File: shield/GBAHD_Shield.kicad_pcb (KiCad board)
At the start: 2 copper layers, 79.5 x 64.4 mm, 70 parts, among them J1 Conn_01x40, J10 Conn_01x02, J11 Conn_01x05, J2 Conn_02x08_Top_Bottom, J3 Conn_01x20, J4 Conn_02x10_Top_Bottom, J5 Conn_01x34, J6 Conn_02x03_Odd_Even, J7 Conn_01x32, J8 Conn_01x05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

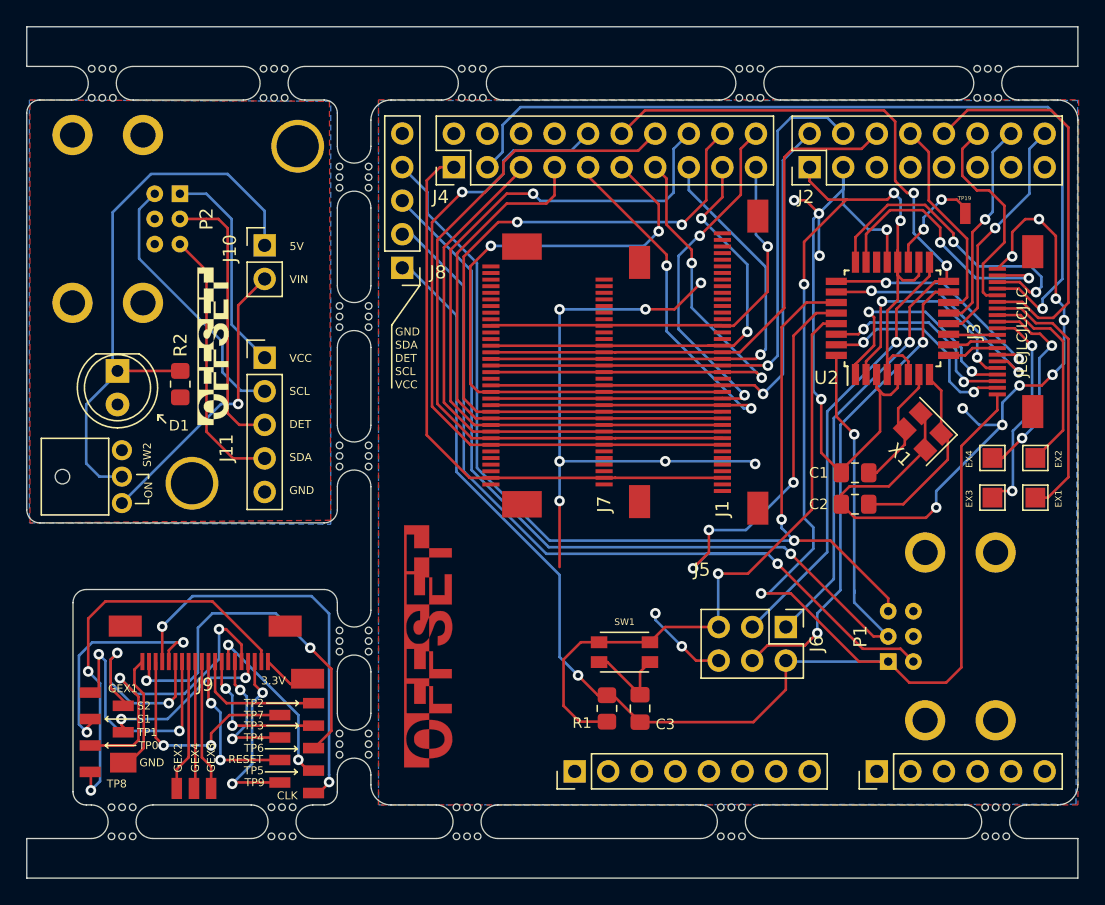
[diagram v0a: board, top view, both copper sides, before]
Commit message: Fixed moved traces
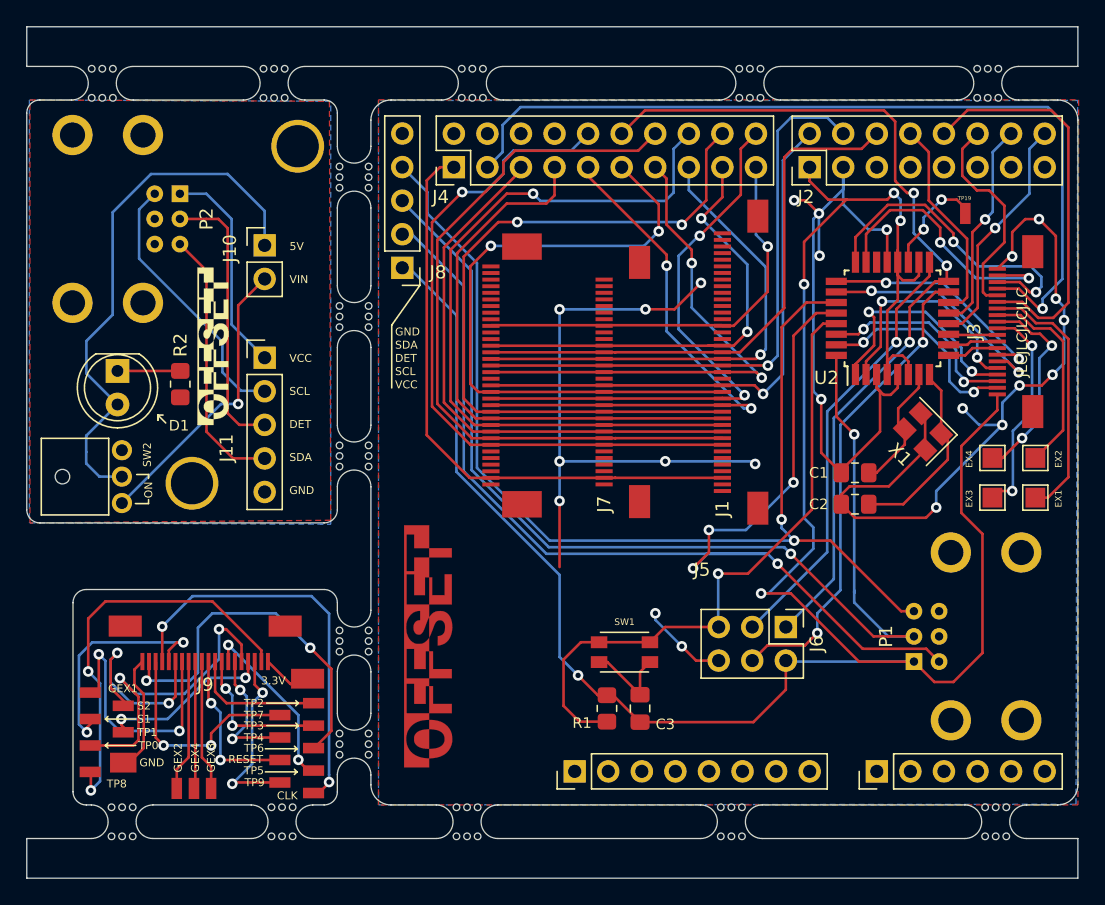
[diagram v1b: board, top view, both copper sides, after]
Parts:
- moved P1 1.94 mm to (158.6, 87.5)
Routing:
- net JOY_DET: track 82.4 -> 86.2 mm
- net GBA_VCC: track 169.8 -> 173.3 mm
- net EXT_5V: track 39.4 -> 41.4 mm
- net JOY_SCL: track 92.7 -> 94.7 mm
- net JOY_SDA: track 82.7 -> 84.1 mm
